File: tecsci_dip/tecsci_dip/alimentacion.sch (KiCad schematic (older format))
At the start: 17 parts, among them IC301 LP2985AIM5-3.3, U301 Regulator_Controller_LM5161

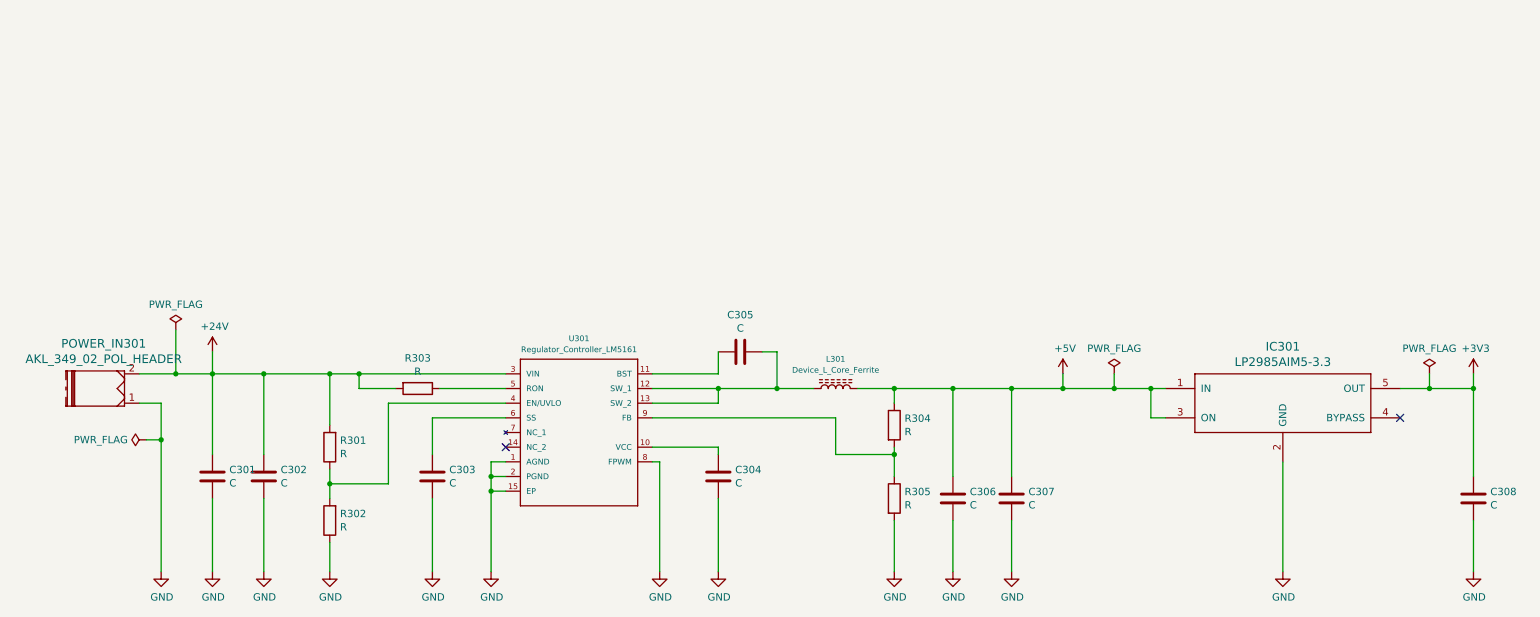
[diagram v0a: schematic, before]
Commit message: add value and footprint
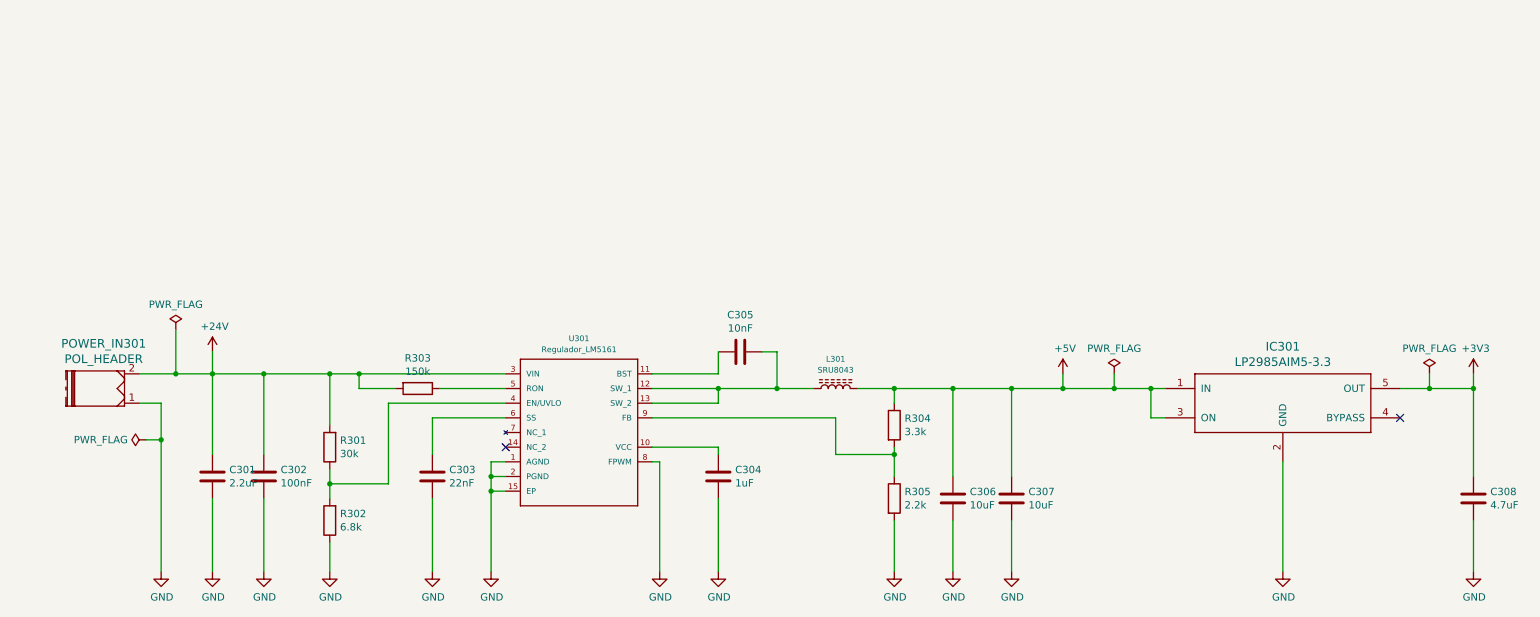
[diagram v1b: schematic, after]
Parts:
- C301: value C -> 2.2uF; footprint (none) -> Capacitor_SMD:C_1206_3216Metric
- C302: value C -> 100nF; footprint (none) -> Capacitor_SMD:C_1206_3216Metric
- C303: value C -> 22nF; footprint (none) -> Capacitor_SMD:C_0603_1608Metric
- C304: value C -> 1uF; footprint (none) -> Capacitor_SMD:C_0603_1608Metric
- C305: value C -> 10nF; footprint (none) -> Capacitor_SMD:C_0603_1608Metric
- C306, C307: value C -> 10uF; footprint (none) -> Capacitor_SMD:C_0805_2012Metric
- C308: value C -> 4.7uF
- L301: value Device_L_Core_Ferrite -> SRU8043; footprint (none) -> Inductor_SMD:L_Bourns-SRU8043
- POWER_IN301: value AKL_349_02_POL_HEADER -> POL_HEADER
- R301: value R -> 30k; footprint (none) -> Capacitor_SMD:C_0805_2012Metric
- R302: value R -> 6.8k; footprint (none) -> Resistor_SMD:R_0603_1608Metric
- R303: value R -> 150k; footprint (none) -> Resistor_SMD:R_0805_2012Metric
- R304: value R -> 3.3k; footprint (none) -> Resistor_SMD:R_0603_1608Metric
- R305: value R -> 2.2k; footprint (none) -> Resistor_SMD:R_0603_1608Metric
- U301: value Regulator_Controller_LM5161 -> Regulador_LM5161
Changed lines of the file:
@@
 P 4200 3850
 F 0 "U301" H 4200 4491 39  0000 C CNN
-F 1 "Regulator_Controller_LM5161" H 4200 4416 39  0000 C CNN
+F 1 "Regulador_LM5161" H 4200 4416 39  0000 C CNN
 F 2 "Package_SO:TSSOP-14-1EP_4.4x5mm_P0.65mm" H 4200 3850 39  0001 C CNN
 F 3 "" H 4200 3850 39  0001 C CNN
@@
 P 3200 4150
 F 0 "C303" H 3315 4196 50  0000 L CNN
-F 1 "C" H 3315 4105 50  0000 L CNN
-F 2 "" H 3238 4000 50  0001 C CNN
+F 1 "22nF" H 3315 4105 50  0000 L CNN
+F 2 "Capacitor_SMD:C_0603_1608Metric" H 3238 4000 50  0001 C CNN
 F 3 "~" H 3200 4150 50  0001 C CNN
 	1    3200 4150
@@
 P 2050 4150
 F 0 "C302" H 2165 4196 50  0000 L CNN
-F 1 "C" H 2165 4105 50  0000 L CNN
-F 2 "" H 2088 4000 50  0001 C CNN
+F 1 "100nF" H 2165 4105 50  0000 L CNN
+F 2 "Capacitor_SMD:C_1206_3216Metric" H 2088 4000 50  0001 C CNN
 F 3 "~" H 2050 4150 50  0001 C CNN
 	1    2050 4150
@@
 P 1700 4150
 F 0 "C301" H 1815 4196 50  0000 L CNN
-F 1 "C" H 1815 4105 50  0000 L CNN
-F 2 "" H 1738 4000 50  0001 C CNN
+F 1 "2.2uF" H 1815 4105 50  0000 L CNN
+F 2 "Capacitor_SMD:C_1206_3216Metric" H 1738 4000 50  0001 C CNN
 F 3 "~" H 1700 4150 50  0001 C CNN
 	1    1700 4150
@@
 P 5150 4150
 F 0 "C304" H 5265 4196 50  0000 L CNN
-F 1 "C" H 5265 4105 50  0000 L CNN
-F 2 "" H 5188 4000 50  0001 C CNN
+F 1 "1uF" H 5265 4105 50  0000 L CNN
+F 2 "Capacitor_SMD:C_0603_1608Metric" H 5188 4000 50  0001 C CNN
 F 3 "~" H 5150 4150 50  0001 C CNN
 	1    5150 4150
@@
 P 6750 4300
 F 0 "C306" H 6865 4346 50  0000 L CNN
-F 1 "C" H 6865 4255 50  0000 L CNN
-F 2 "" H 6788 4150 50  0001 C CNN
+F 1 "10uF" H 6865 4255 50  0000 L CNN
+F 2 "Capacitor_SMD:C_0805_2012Metric" H 6788 4150 50  0001 C CNN
 F 3 "~" H 6750 4300 50  0001 C CNN
 	1    6750 4300
@@
 P 7150 4300
 F 0 "C307" H 7265 4346 50  0000 L CNN
-F 1 "C" H 7265 4255 50  0000 L CNN
-F 2 "" H 7188 4150 50  0001 C CNN
+F 1 "10uF" H 7265 4255 50  0000 L CNN
+F 2 "Capacitor_SMD:C_0805_2012Metric" H 7188 4150 50  0001 C CNN
 F 3 "~" H 7150 4300 50  0001 C CNN
 	1    7150 4300
@@
 P 5300 3300
 F 0 "C305" V 5048 3300 50  0000 C CNN
-F 1 "C" V 5139 3300 50  0000 C CNN
-F 2 "" H 5338 3150 50  0001 C CNN
+F 1 "10nF" V 5139 3300 50  0000 C CNN
+F 2 "Capacitor_SMD:C_0603_1608Metric" H 5338 3150 50  0001 C CNN
 F 3 "~" H 5300 3300 50  0001 C CNN
 	1    5300 3300
@@
 P 5950 3550
 F 0 "L301" V 6151 3550 39  0000 C CNN
-F 1 "Device_L_Core_Ferrite" V 6076 3550 39  0000 C CNN
-F 2 "" H 5950 3550 50  0001 C CNN
+F 1 "SRU8043" V 6076 3550 39  0000 C CNN
+F 2 "Inductor_SMD:L_Bourns-SRU8043" H 5950 3550 50  0001 C CNN
 F 3 "" H 5950 3550 50  0001 C CNN
 	1    5950 3550
@@
 P 6350 3800
 F 0 "R304" H 6420 3846 50  0000 L CNN
-F 1 "R" H 6420 3755 50  0000 L CNN
-F 2 "" V 6280 3800 50  0001 C CNN
+F 1 "3.3k" H 6420 3755 50  0000 L CNN
+F 2 "Resistor_SMD:R_0603_1608Metric" V 6280 3800 50  0001 C CNN
 F 3 "~" H 6350 3800 50  0001 C CNN
 	1    6350 3800
@@
 P 6350 4300
 F 0 "R305" H 6420 4346 50  0000 L CNN
-F 1 "R" H 6420 4255 50  0000 L CNN
-F 2 "" V 6280 4300 50  0001 C CNN
+F 1 "2.2k" H 6420 4255 50  0000 L CNN
+F 2 "Resistor_SMD:R_0603_1608Metric" V 6280 4300 50  0001 C CNN
 F 3 "~" H 6350 4300 50  0001 C CNN
 	1    6350 4300
@@
 P 3100 3550
 F 0 "R303" V 2893 3550 50  0000 C CNN
-F 1 "R" V 2984 3550 50  0000 C CNN
-F 2 "" V 3030 3550 50  0001 C CNN
+F 1 "150k" V 2984 3550 50  0000 C CNN
+F 2 "Resistor_SMD:R_0805_2012Metric" V 3030 3550 50  0001 C CNN
 F 3 "~" H 3100 3550 50  0001 C CNN
 	1    3100 3550
@@
 P 2500 3950
 F 0 "R301" H 2430 3904 50  0000 R CNN
-F 1 "R" H 2430 3995 50  0000 R CNN
-F 2 "" V 2430 3950 50  0001 C CNN
+F 1 "30k" H 2430 3995 50  0000 R CNN
+F 2 "Capacitor_SMD:C_0805_2012Metric" V 2430 3950 50  0001 C CNN
 F 3 "~" H 2500 3950 50  0001 C CNN
 	1    2500 3950
@@
 P 2500 4450
 F 0 "R302" H 2430 4404 50  0000 R CNN
-F 1 "R" H 2430 4495 50  0000 R CNN
-F 2 "" V 2430 4450 50  0001 C CNN
+F 1 "6.8k" H 2430 4495 50  0000 R CNN
+F 2 "Resistor_SMD:R_0603_1608Metric" V 2430 4450 50  0001 C CNN
 F 3 "~" H 2500 4450 50  0001 C CNN
 	1    2500 4450
@@
 P 10300 4300
 F 0 "C308" H 10415 4346 50  0000 L CNN
-F 1 "C" H 10415 4255 50  0000 L CNN
+F 1 "4.7uF" H 10415 4255 50  0000 L CNN
 F 2 "TMC5130-Eval_v15:0603" H 10338 4150 50  0001 C CNN
 F 3 "~" H 10300 4300 50  0001 C CNN
@@
 P 900 3550
 F 0 "POWER_IN301" H 842 3244 59  0000 C CNN
-F 1 "AKL_349_02_POL_HEADER" H 842 3349 59  0000 C CNN
+F 1 "POL_HEADER" H 842 3349 59  0000 C CNN
 F 2 "TMC5130-Eval_v15:AKL349_02_POL" H 900 3550 50  0001 C CNN
 F 3 "" H 900 3550 50  0001 C CNN

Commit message: agrego valor faltantes en esquematico
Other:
- note added: "Etapa Reguladora de Tensión\nEntrada 24-46Volt\nSalida 5V\nSalida 3V"
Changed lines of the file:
@@
 $EndDescr
-$Comp
-L Ponchobrücke-cache:Regulator_Controller_LM5161 U301
-U 1 1 5D9BFA46
-P 4200 3850
-F 0 "U301" H 4200 4491 39  0000 C CNN
-F 1 "Regulador_LM5161" H 4200 4416 39  0000 C CNN
-F 2 "Package_SO:TSSOP-14-1EP_4.4x5mm_P0.65mm" H 4200 3850 39  0001 C CNN
-F 3 "" H 4200 3850 39  0001 C CNN
-	1    4200 3850
-	1    0    0    -1
-$EndComp
 $Comp
 L Device:C C303
@@
 	10300 3450 10300 3550
 Connection ~ 10300 3550
+$Comp
+L Ponchobrücke-cache:Regulator_Controller_LM5161 U301
+U 1 1 5D9BFA46
+P 4200 3850
+F 0 "U301" H 4200 4491 39  0000 C CNN
+F 1 "Regulador_LM5161" H 4200 4416 39  0000 C CNN
+F 2 "Package_SO:TSSOP-14-1EP_4.4x5mm_P0.65mm" H 4200 3850 39  0001 C CNN
+F 3 "" H 4200 3850 39  0001 C CNN
+	1    4200 3850
+	1    0    0    -1
+$EndComp
+Text Notes 1400 1550 0    50   Italic 10
+Etapa Reguladora de Tensión\nEntrada 24-46Volt\nSalida 5V\nSalida 3V
 $EndSCHEMATC

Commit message: update board
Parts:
- removed C308: 4.7uF, TMC5130-Eval_v15:0603, symbol Device:C
- removed IC301: LP2985AIM5-3.3, TMC5130-Eval_v15:SOT23-5, symbol TMC5130-Eval_v15-eagle-import:LP2985AIM5-3.3
- added D301: PMEG6010CEH, Diode_SMD:D_SOD-123, symbol Diode:PMEG6010CEH
- C303, C304, C305: footprint Capacitor_SMD:C_0603_1608Metric -> Capacitor_SMD:C_0805_2012Metric
- R302, R304, R305: footprint Resistor_SMD:R_0603_1608Metric -> Resistor_SMD:R_0805_2012Metric
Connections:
- net +5V: no longer names the net of C306.1, C307.1, L301.2, R304.1
- net +5V: now also D301.2 (A)
- new net +5VD: D301.1 (K)
- no-connect marks 2 -> 1
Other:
- note added: "Etapa Reguladora de Tensión\nEntrada 24-46Volt\nSalida 5V hacia integrado TMC130\nSalida 5V hacia microcontrolador con diodo de protección"
- note removed: "Etapa Reguladora de Tensión\nEntrada 24-46Volt\nSalida 5V\nSalida 3V"
- moved on the sheet: C301, C302, C303, C304, C305, C306, C307, L301, POWER_IN301, R301, R302, R303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

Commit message: add fiduciales
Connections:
- no-connect marks 1 -> 2
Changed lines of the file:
@@
 Wire Wire Line
 	2550 3850 2550 4750
-$Comp
-L Ponchobrücke-cache:Regulator_Controller_LM5161 U301
-U 1 1 5D9BFA46
-P 5400 3800
-F 0 "U301" H 5400 4441 39  0000 C CNN
-F 1 "Regulador_LM5161" H 5400 4366 39  0000 C CNN
-F 2 "Package_SO:TSSOP-14-1EP_4.4x5mm_P0.65mm" H 5400 3800 39  0001 C CNN
-F 3 "" H 5400 3800 39  0001 C CNN
-	1    5400 3800
-	1    0    0    -1
-$EndComp
 Text Notes 1400 1550 0    87   Italic 17
 Etapa Reguladora de Tensión\nEntrada 24-46Volt\nSalida 5V hacia integrado TMC130\nSalida 5V hacia microcontrolador con diodo de protección
@@
 Wire Wire Line
 	8350 3500 9050 3500
+$Comp
+L Ponchobrücke-cache:Regulator_Controller_LM5161 U301
+U 1 1 5D9BFA46
+P 5400 3800
+F 0 "U301" H 5400 4441 39  0000 C CNN
+F 1 "Regulador_LM5161" H 5400 4366 39  0000 C CNN
+F 2 "Package_SO:TSSOP-14-1EP_4.4x5mm_P0.65mm" H 5400 3800 39  0001 C CNN
+F 3 "" H 5400 3800 39  0001 C CNN
+	1    5400 3800
+	1    0    0    -1
+$EndComp
+NoConn ~ 4900 3800
 $EndSCHEMATC

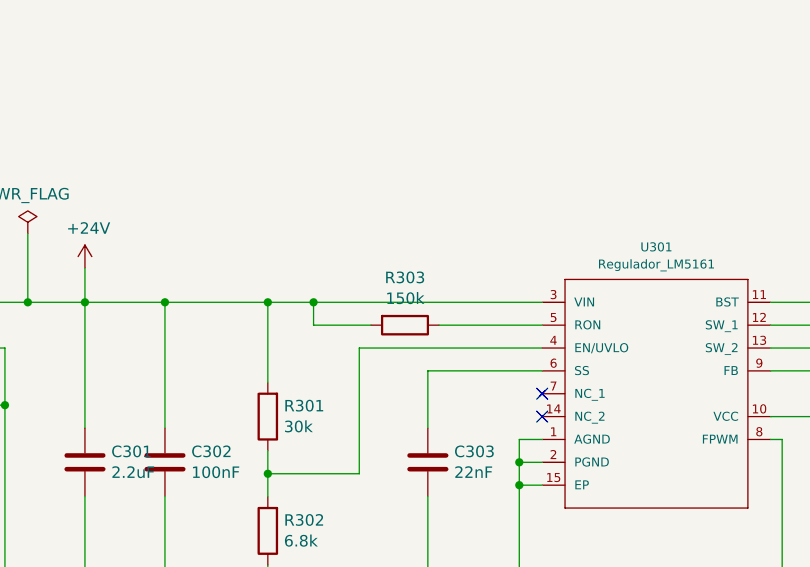
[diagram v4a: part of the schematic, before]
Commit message: Se corrigen todos los errores marcados por el profesor, excepto pasar a footprint conectores de ESP32, ya que la v2 contendra al CI
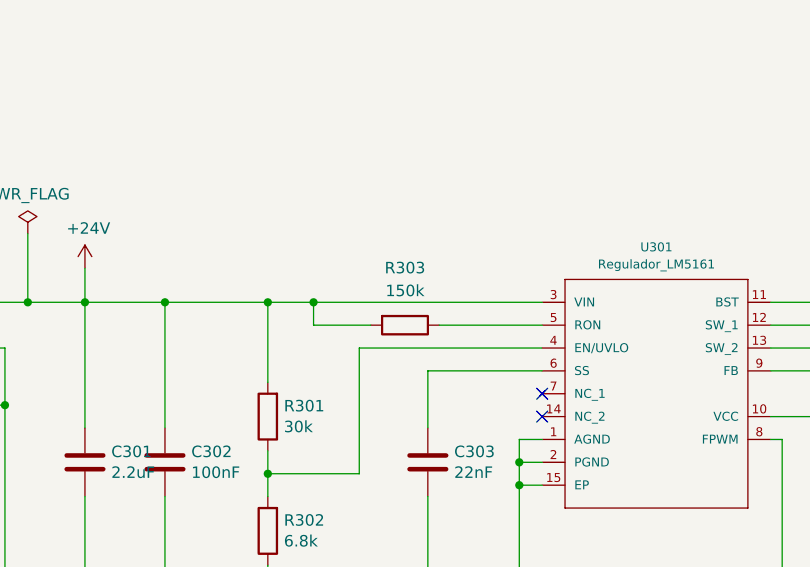
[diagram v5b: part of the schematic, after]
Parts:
- D301: manf (none) -> Nexperia USA Inc.; manf# (none) -> PMEG6010CEH,115
- L301: digikey# (none) -> SRU8043-100YTR-ND; manf (none) -> Bourns Inc.; manf# (none) -> SRU8043-100Y
- U301: digikey# (none) -> 296-47791-2-ND; manf (none) -> Texas Instruments; manf# (none) -> LM5161QPWPRQ1
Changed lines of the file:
@@
 Date "2019-10-02"
 Rev "1"
-Comp "Tecsci"
-Comment1 "Martin Abel Gambarotta"
-Comment2 "Revisor: Mariano Campos"
-Comment3 ""
-Comment4 ""
+Comp "Tecsci  Tecnología para Ciencia                            Licensed under CERN OHL v.1.2"
+Comment1 "Ing. Electrónico Martin Abel Gambarotta"
+Comment2 ""
+Comment3 "Revisor: Mariano Campos"
+Comment4 "Revisor: Diego Brengi"
 $EndDescr
 $Comp
@@
 F 1 "SRU8043" V 7276 3500 39  0000 C CNN
 F 2 "Inductor_SMD:L_Bourns-SRU8043" H 7150 3500 50  0001 C CNN
-F 3 "" H 7150 3500 50  0001 C CNN
+F 3 "https://www.bourns.com/docs/Product-Datasheets/SRU8043.pdf" H 7150 3500 50  0001 C CNN
+F 4 "SRU8043-100YTR-ND" H 7150 3500 50  0001 C CNN "digikey#"
+F 5 "Bourns Inc." H 7150 3500 50  0001 C CNN "manf"
+F 6 "SRU8043-100Y" H 7150 3500 50  0001 C CNN "manf#"
 	1    7150 3500
 	0    -1   -1   0
@@
 U 1 1 5D9C7F28
 P 4300 3500
-F 0 "R303" V 4093 3500 50  0000 C CNN
-F 1 "150k" V 4184 3500 50  0000 C CNN
+F 0 "R303" V 4050 3500 50  0000 C CNN
+F 1 "150k" V 4150 3500 50  0000 C CNN
 F 2 "Resistor_SMD:R_0805_2012Metric" V 4230 3500 50  0001 C CNN
 F 3 "~" H 4300 3500 50  0001 C CNN
@@
 F 2 "Diode_SMD:D_SOD-123" H 9500 3325 50  0001 C CNN
 F 3 "https://assets.nexperia.com/documents/data-sheet/PMEG6010CEH_PMEG6010CEJ.pdf" H 9500 3500 50  0001 C CNN
+F 4 "1727-3848-2-ND
+" H 9500 3500 50  0001 C CNN "digikey#"
+F 5 "Nexperia USA Inc." H 9500 3500 50  0001 C CNN "manf"
+F 6 "PMEG6010CEH,115" H 9500 3500 50  0001 C CNN "manf#"
 	1    9500 3500
 	-1   0    0    1
@@
 F 1 "Regulador_LM5161" H 5400 4366 39  0000 C CNN
 F 2 "Package_SO:TSSOP-14-1EP_4.4x5mm_P0.65mm" H 5400 3800 39  0001 C CNN
-F 3 "" H 5400 3800 39  0001 C CNN
+F 3 "http://www.ti.com/general/docs/suppproductinfo.tsp?distId=10&gotoUrl=http%3A%2F%2Fwww.ti.com%2Flit%2Fgpn%2Flm5161-q1" H 5400 3800 39  0001 C CNN
+F 4 "296-47791-2-ND" H 5400 3800 50  0001 C CNN "digikey#"
+F 5 "Texas Instruments" H 5400 3800 50  0001 C CNN "manf"
+F 6 "LM5161QPWPRQ1" H 5400 3800 50  0001 C CNN "manf#"
 	1    5400 3800
 	1    0    0    -1

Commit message: arreglo en alimentacion.sch , habria con error en archivo
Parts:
- D301: digikey# (none) -> 1727-3848-2-ND
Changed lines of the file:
@@
 F 2 "Diode_SMD:D_SOD-123" H 9500 3325 50  0001 C CNN
 F 3 "https://assets.nexperia.com/documents/data-sheet/PMEG6010CEH_PMEG6010CEJ.pdf" H 9500 3500 50  0001 C CNN
-F 4 "1727-3848-2-ND
-" H 9500 3500 50  0001 C CNN "digikey#"
+F 4 "1727-3848-2-ND" H 9500 3500 50  0001 C CNN "digikey#"
 F 5 "Nexperia USA Inc." H 9500 3500 50  0001 C CNN "manf"
 F 6 "PMEG6010CEH,115" H 9500 3500 50  0001 C CNN "manf#"
